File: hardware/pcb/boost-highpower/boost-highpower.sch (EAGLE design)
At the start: 28 parts

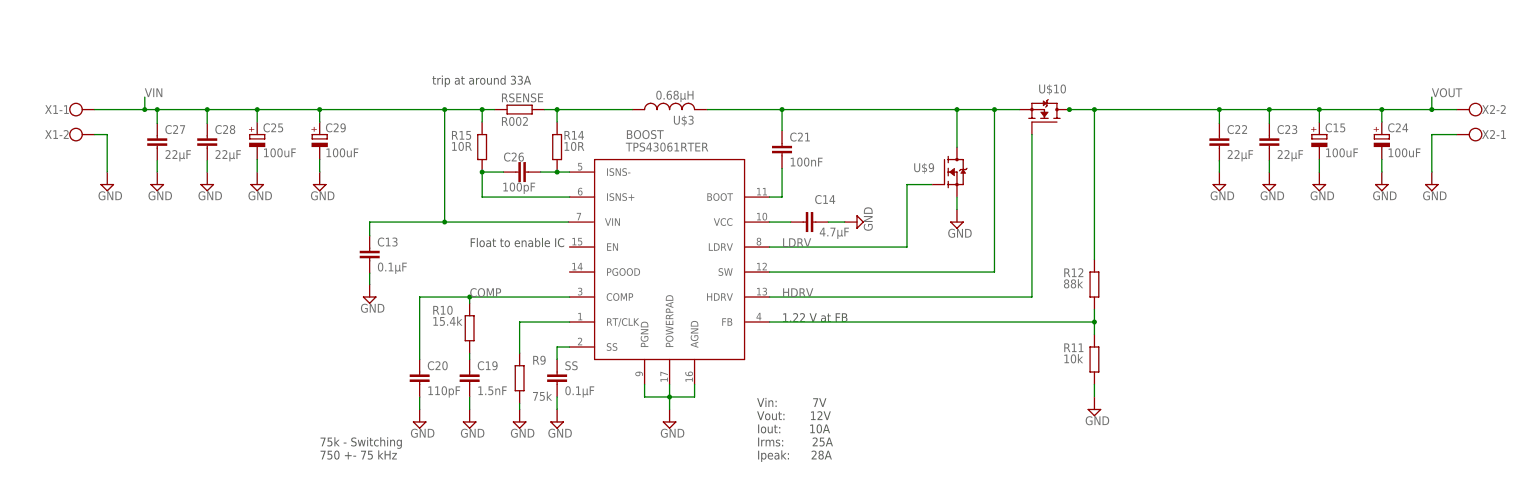
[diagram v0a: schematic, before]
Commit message: Moved components to a first place
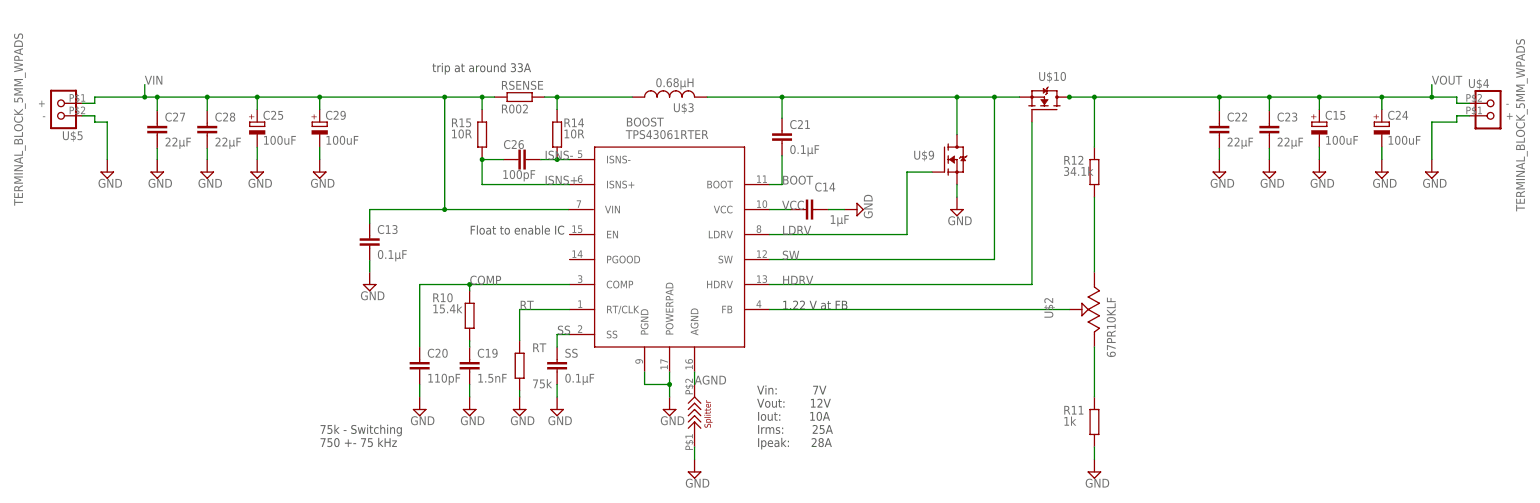
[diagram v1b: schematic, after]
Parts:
- removed R9: 75k, rcl:R-EU_R0603
- removed X1, X2: (no value), con-wago-500:W237-102
- added RT: 75k, rcl:R-EU_R0603
- added U$1: SPLITTER, PowerManagement:SPLITTER
- added U$2: 67PR10KLF, Passive:67PR10KLF
- added U$4, U$5: TERMINAL_BLOCK_5MM_WPADS, Connectors:TERMINAL_BLOCK_5MM_WPADS
- C14: value 4.7µF -> 1µF; device rcl:C-EUC0805 -> rcl:C-EUC0603
- C19, C20, C26, SS: device rcl:C-EUC0805 -> rcl:C-EUC0603
- C21: value 100nF -> 0.1µF
- R11: value 10k -> 1k
- R12: value 88k -> 34.1k
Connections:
- net N$12 renamed SS
- net N$16 renamed BOOT
- net N$19 renamed SW
- net N$2 renamed VCC
- net N$22 renamed ISNS-
- net N$23 renamed ISNS+
- removed net N$11: BOOST.RT/CLK, R9.2
- new net AGND: BOOST.AGND, U$1.2
- new net N$3: R12.1, U$2.3
- new net N$4: R11.2, U$2.1
- new net RT: BOOST.RT/CLK, RT.2
- net GND: now also RT.1, U$1.1, U$4.+, U$5.-; no longer BOOST.AGND, R9.1, X1-2.KL, X2-1.KL
- net N$20: now also U$2.2; no longer R11.2, R12.1
- net VIN: now also U$5.+; no longer X1-1.KL
- net VOUT: now also U$4.-; no longer X2-2.KL
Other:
- moved on the sheet: BOOST, C13, C14, C15, C19, C20, C21, C22, C23, C24, C25, C26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

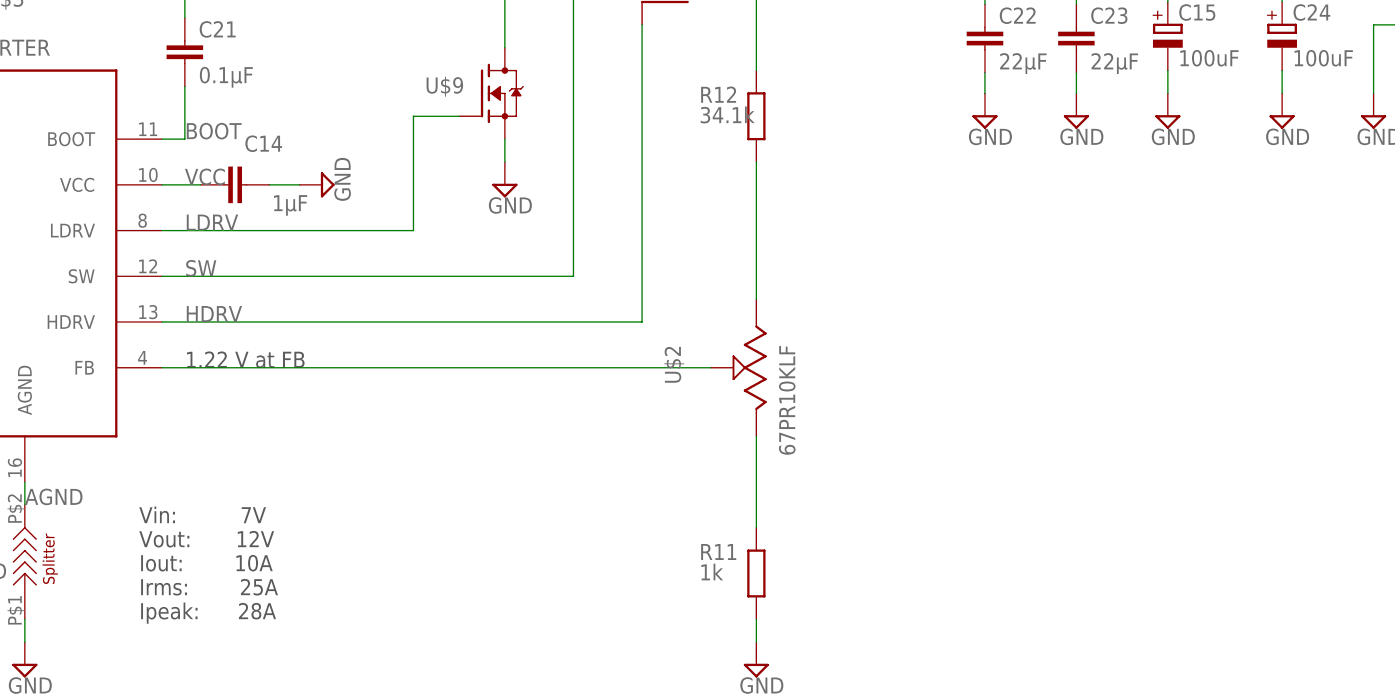
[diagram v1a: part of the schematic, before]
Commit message: Routed board
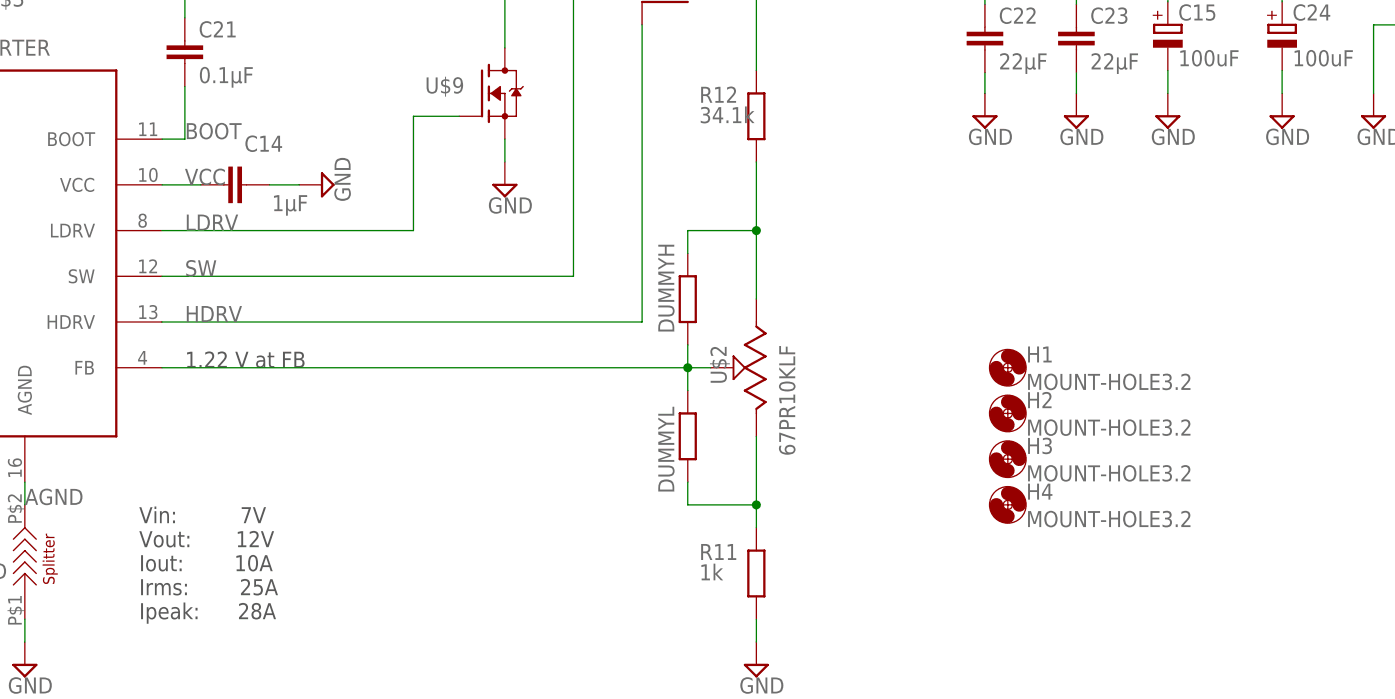
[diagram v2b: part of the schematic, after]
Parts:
- added DUMMYH, DUMMYL: (no value), rcl:R-EU_R0201
- added H1, H2, H3, H4: MOUNT-HOLE3.2, holes:MOUNT-HOLE3.2
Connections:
- net N$20: now also DUMMYH.1, DUMMYL.2
- net N$3: now also DUMMYH.2
- net N$4: now also DUMMYL.1

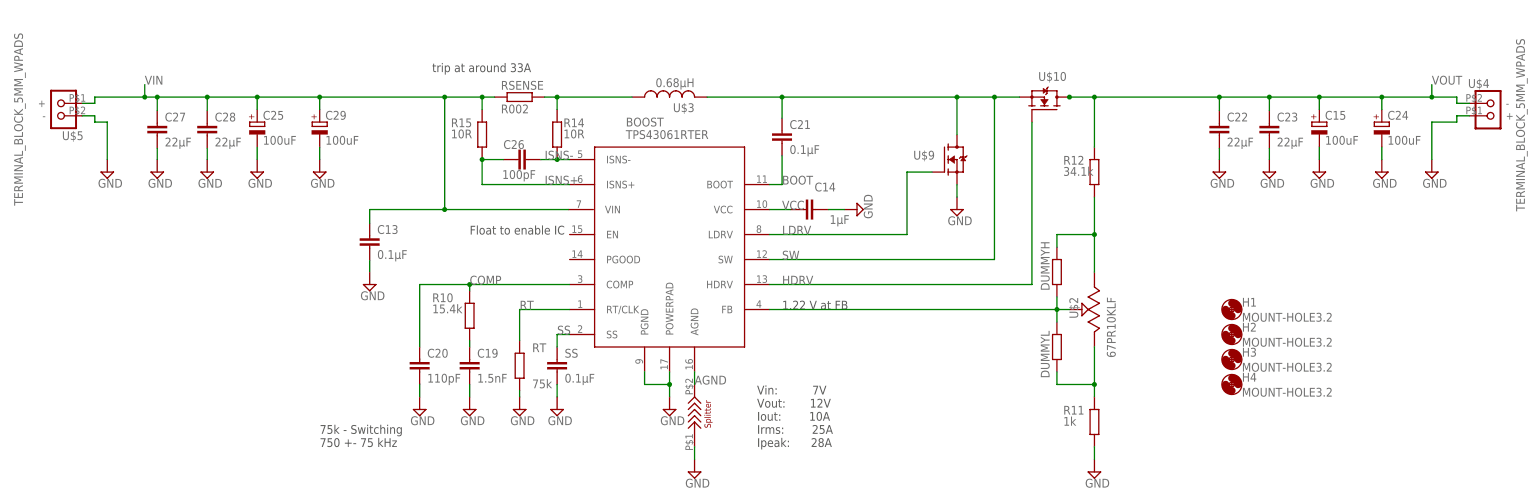
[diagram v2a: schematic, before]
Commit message: Changed cap to 50V and 100V to meet requirement
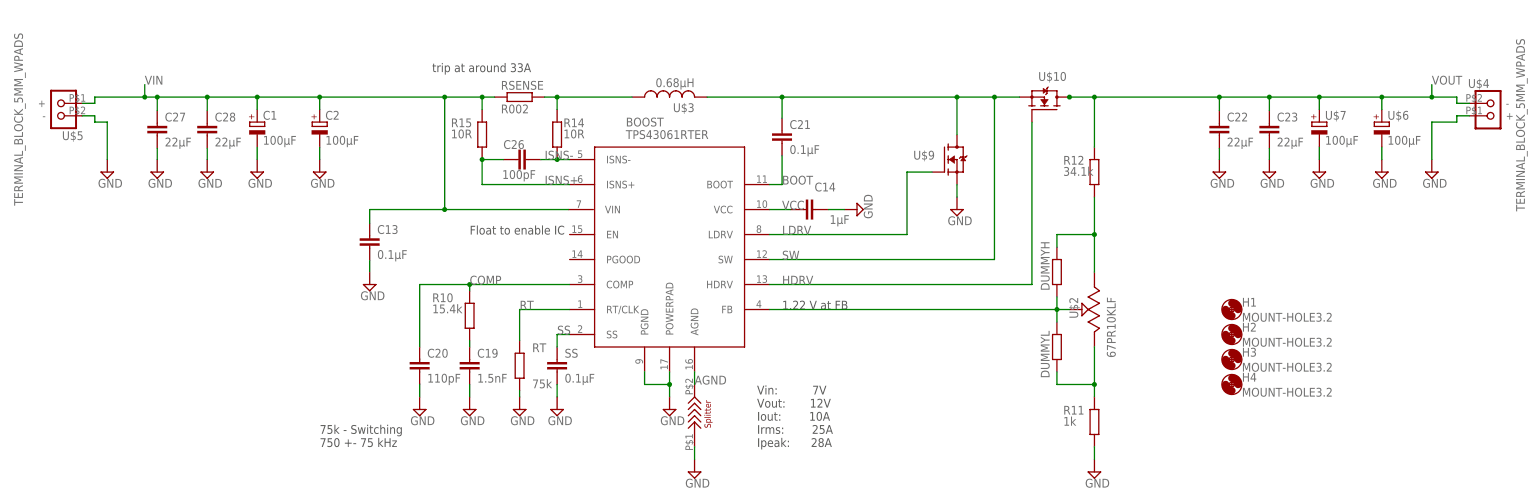
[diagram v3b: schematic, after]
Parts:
- removed C15, C24, C25, C29: 100uF, Passive:WCAP-ASLL-WEWCAP-ASLL
- added C1, C2: 100µF, Passive:WCAP-ASLL-WE50V100µF
- added U$6, U$7: 100µF, Passive:CAP_VZH
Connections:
- net GND: now also C1.-, C2.-, U$6.-, U$7.-; no longer C15.-, C24.-, C25.-, C29.-
- net VIN: now also C1.+, C2.+; no longer C25.+, C29.+
- net VOUT: now also U$6.+, U$7.+; no longer C15.+, C24.+
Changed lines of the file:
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@@
 <part name="SUPPLY22" library="supply2" library_urn="urn:adsk.eagle:library:372" deviceset="GND" device=""/>
 <part name="RSENSE" library="rcl" library_urn="urn:adsk.eagle:library:334" deviceset="R-EU_" device="R2512W" package3d_urn="urn:adsk.eagle:package:23565/2" value="R002"/>
-<part name="C15" library="Passive" library_urn="urn:adsk.eagle:library:17612641" deviceset="WCAP-ASLL-WE" device="WCAP-ASLL" package3d_urn="urn:adsk.eagle:package:17897073/3" value="100uF"/>
-<part name="C24" library="Passive" library_urn="urn:adsk.eagle:library:17612641" deviceset="WCAP-ASLL-WE" device="WCAP-ASLL" package3d_urn="urn:adsk.eagle:package:17897073/3" value="100uF"/>
-<part name="C25" library="Passive" library_urn="urn:adsk.eagle:library:17612641" deviceset="WCAP-ASLL-WE" device="WCAP-ASLL" package3d_urn="urn:adsk.eagle:package:17897073/3" value="100uF"/>
-<part name="C29" library="Passive" library_urn="urn:adsk.eagle:library:17612641" deviceset="WCAP-ASLL-WE" device="WCAP-ASLL" package3d_urn="urn:adsk.eagle:package:17897073/3" value="100uF"/>
 <part name="FRAME1" library="frames" library_urn="urn:adsk.eagle:library:229" deviceset="A3L-LOC" device=""/>
 <part name="SUPPLY1" library="supply2" library_urn="urn:adsk.eagle:library:372" deviceset="GND" device=""/>
@@
 <part name="H3" library="holes" library_urn="urn:adsk.eagle:library:237" deviceset="MOUNT-HOLE" device="3.2" package3d_urn="urn:adsk.eagle:package:14275/1"/>
 <part name="H4" library="holes" library_urn="urn:adsk.eagle:library:237" deviceset="MOUNT-HOLE" device="3.2" package3d_urn="urn:adsk.eagle:package:14275/1"/>
+<part name="C1" library="Passive" library_urn="urn:adsk.eagle:library:17612641" deviceset="WCAP-ASLL-WE" device="50V100µF" package3d_urn="urn:adsk.eagle:package:18738374/1" value="100µF"/>
+<part name="C2" library="Passive" library_urn="urn:adsk.eagle:library:17612641" deviceset="WCAP-ASLL-WE" device="50V100µF" package3d_urn="urn:adsk.eagle:package:18738374/1" value="100µF"/>
+<part name="U$6" library="Passive" library_urn="urn:adsk.eagle:library:17612641" deviceset="CAP_VZH" device="" package3d_urn="urn:adsk.eagle:package:18738359/1" value="100µF"/>
+<part name="U$7" library="Passive" library_urn="urn:adsk.eagle:library:17612641" deviceset="CAP_VZH" device="" package3d_urn="urn:adsk.eagle:package:18738359/1" value="100µF"/>
 </parts>
 <sheets>
@@
 <attribute name="VALUE" x="-34.29" y="27.178" size="1.778" layer="96"/>
 </instance>
-<instance part="C15" gate="G$1" x="134.62" y="22.86" smashed="yes" grouprefs="BOOST-MODULE">
-<attribute name="NAME" x="133.223" y="25.8826" size="1.778" layer="95"/>
-<attribute name="VALUE" x="133.223" y="20.8026" size="1.778" layer="96"/>
-</instance>
-<instance part="C24" gate="G$1" x="147.32" y="22.86" smashed="yes" grouprefs="BOOST-MODULE">
-<attribute name="NAME" x="145.923" y="25.8826" size="1.778" layer="95"/>
-<attribute name="VALUE" x="145.923" y="20.8026" size="1.778" layer="96"/>
-</instance>
-<instance part="C25" gate="G$1" x="-81.28" y="22.86" smashed="yes" grouprefs="BOOST-MODULE">
-<attribute name="NAME" x="-82.677" y="25.8826" size="1.778" layer="95"/>
-<attribute name="VALUE" x="-82.677" y="20.8026" size="1.778" layer="96"/>
-</instance>
-<instance part="C29" gate="G$1" x="-68.58" y="22.86" smashed="yes" grouprefs="BOOST-MODULE">
-<attribute name="NAME" x="-69.977" y="25.8826" size="1.778" layer="95"/>
-<attribute name="VALUE" x="-69.977" y="20.8026" size="1.778" layer="96"/>
-</instance>
 <instance part="FRAME1" gate="G$1" x="-167.64" y="-132.08" smashed="yes">
 <attribute name="DRAWING_NAME" x="176.53" y="-116.84" size="2.54" layer="94"/>
@@
 <attribute name="NAME" x="116.332" y="-27.3558" size="1.778" layer="95"/>
 <attribute name="VALUE" x="116.332" y="-30.4038" size="1.778" layer="96"/>
+</instance>
+<instance part="C1" gate="G$1" x="-81.28" y="22.86" smashed="yes">
+<attribute name="NAME" x="-82.677" y="25.8826" size="1.778" layer="95"/>
+<attribute name="VALUE" x="-82.677" y="20.8026" size="1.778" layer="96"/>
+</instance>
+<instance part="C2" gate="G$1" x="-68.58" y="22.86" smashed="yes">
+<attribute name="NAME" x="-69.977" y="25.8826" size="1.778" layer="95"/>
+<attribute name="VALUE" x="-69.977" y="20.8026" size="1.778" layer="96"/>
+</instance>
+<instance part="U$6" gate="G$1" x="147.32" y="22.86" smashed="yes">
+<attribute name="NAME" x="145.923" y="25.8826" size="1.778" layer="95"/>
+<attribute name="VALUE" x="145.923" y="20.8026" size="1.778" layer="96"/>
+</instance>
+<instance part="U$7" gate="G$1" x="134.62" y="22.86" smashed="yes">
+<attribute name="NAME" x="133.223" y="25.8826" size="1.778" layer="95"/>
+<attribute name="VALUE" x="133.223" y="20.8026" size="1.778" layer="96"/>
 </instance>
 </instances>
@@
 <pinref part="SUPPLY36" gate="GND" pin="GND"/>
 <wire x1="144.78" y1="17.78" x2="144.78" y2="20.32" width="0.1524" layer="91" grouprefs="BOOST-MODULE"/>
-<pinref part="C24" gate="G$1" pin="-"/>
+<pinref part="U$6" gate="G$1" pin="-"/>
 </segment>
 <segment>
 <pinref part="SUPPLY35" gate="GND" pin="GND"/>
 <wire x1="132.08" y1="20.32" x2="132.08" y2="17.78" width="0.1524" layer="91" grouprefs="BOOST-MODULE"/>
-<pinref part="C15" gate="G$1" pin="-"/>
+<pinref part="U$7" gate="G$1" pin="-"/>
 </segment>
 <segment>
@@
 <pinref part="SUPPLY40" gate="GND" pin="GND"/>
 <wire x1="-71.12" y1="17.78" x2="-71.12" y2="20.32" width="0.1524" layer="91" grouprefs="BOOST-MODULE"/>
-<pinref part="C29" gate="G$1" pin="-"/>
+<pinref part="C2" gate="G$1" pin="-"/>
 </segment>
 <segment>
 <pinref part="SUPPLY39" gate="GND" pin="GND"/>
 <wire x1="-83.82" y1="20.32" x2="-83.82" y2="17.78" width="0.1524" layer="91" grouprefs="BOOST-MODULE"/>
-<pinref part="C25" gate="G$1" pin="-"/>
+<pinref part="C1" gate="G$1" pin="-"/>
 </segment>
 <segment>
@@
 <pinref part="U$10" gate="G$1" pin="D"/>
 <junction x="81.28" y="30.48" grouprefs="BOOST-MODULE"/>
-<pinref part="C15" gate="G$1" pin="+"/>
-<pinref part="C24" gate="G$1" pin="+"/>
 <label x="154.94" y="33.02" size="1.778" layer="95" grouprefs="BOOST-MODULE"/>
 <wire x1="160.02" y1="30.48" x2="154.94" y2="30.48" width="0.1524" layer="91" grouprefs="BOOST-MODULE"/>
@@
 <wire x1="162.56" y1="29.21" x2="160.02" y2="29.21" width="0.1524" layer="91" grouprefs="BOOST-MODULE"/>
 <wire x1="160.02" y1="29.21" x2="160.02" y2="30.48" width="0.1524" layer="91" grouprefs="BOOST-MODULE"/>
+<pinref part="U$6" gate="G$1" pin="+"/>
+<pinref part="U$7" gate="G$1" pin="+"/>
 </segment>
 </net>
@@
 <junction x="-45.72" y="7.62" grouprefs="BOOST-MODULE"/>
 <pinref part="RSENSE" gate="G$1" pin="1"/>
-<pinref part="C25" gate="G$1" pin="+"/>
-<pinref part="C29" gate="G$1" pin="+"/>
 <label x="-106.68" y="33.02" size="1.778" layer="95" grouprefs="BOOST-MODULE"/>
 <wire x1="-106.68" y1="30.48" x2="-106.68" y2="33.02" width="0.1524" layer="91" grouprefs="BOOST-MODULE"/>
@@
 <wire x1="-119.38" y1="29.21" x2="-116.84" y2="29.21" width="0.1524" layer="91" grouprefs="BOOST-MODULE"/>
 <wire x1="-116.84" y1="29.21" x2="-116.84" y2="30.48" width="0.1524" layer="91" grouprefs="BOOST-MODULE"/>
-</segment>
-</net>
+<pinref part="C1" gate="G$1" pin="+"/>
+<pinref part="C2" gate="G$1" pin="+"/>
+</segment>
+</net>
